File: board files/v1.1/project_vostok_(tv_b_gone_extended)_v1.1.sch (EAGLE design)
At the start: 25 parts, among them IC1 ATMEGA644PV-10PU, IC2 MCP1825S-3302E_DB, Q5 MPS2907A, T1 2N3904, T2 2N3904, T3 2N3904, T4 2N3904, U1 PEC11R-4015F-S0024

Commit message: modify port
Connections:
- removed net N$1: PORTC.10
- removed net N$2: PORTA.10
- new net N$4: R3.2, S1.2
- net GND: now also PORTA.2, PORTC.2
- net PA0: now also PORTA.10; no longer PORTA.1
- net PA1: now also PORTA.9; no longer PORTA.2
- net PA2: now also PORTA.8; no longer PORTA.3
- net PA3: now also PORTA.7; no longer PORTA.4
- net PA4: now also PORTA.6; no longer PORTA.5
- net PA5: now also PORTA.5; no longer PORTA.6
- net PA6: now also PORTA.4; no longer PORTA.7
- net PA7: now also PORTA.3; no longer PORTA.8
- net PC0: now also PORTC.10; no longer PORTC.1
- net PC1: now also PORTC.9; no longer PORTC.2
- net PC2: now also PORTC.8; no longer PORTC.3
- net PC3: now also PORTC.7; no longer PORTC.4
- net PC4: now also PORTC.6; no longer PORTC.5
- net PC5: now also PORTC.5; no longer PORTC.6
- net PC6: now also PORTC.4; no longer PORTC.7
- net PC7: now also PORTC.3; no longer PORTC.8
- net RESET: no longer R3.2, S1.2
- net VOUT_REG: now also PORTA.1, PORTC.1; no longer PORTA.9, PORTC.9

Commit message: add usb
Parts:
- added R5, R6: 68, rcl:R-EU_0204/7
- added R7: 1.5K, rcl:R-EU_0204/7
- added X1: MINI-USB_SHIELD5P2-32005-601, con-cypressindustries:MINI-USB_SHIELD5P2-32005-601
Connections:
- removed net N$11: IC1.PD0
- removed net N$12: IC1.PD1
- new net N$1: X1G41.1
- new net N$2: R5.1, X1G41.3
- new net N$5: X1G41.4
- new net N$6: R6.1, R7.1, X1G41.2
- new net PD0: IC1.PD0, R2.1
- new net PD1: IC1.PD1, R1.1, U1.1
- net GND: now also X1G41.5
- net PB2: now also R5.2; no longer R1.1, U1.1
- net PB3: now also R6.2; no longer R2.1
- net VIN_REG: now also R7.2
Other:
- note added: "D+"
- note added: "D-"
- note added: "GND"
- note added: "ID"
- note added: "USB"
- note added: "VCC"
- moved on the sheet: BAT_1, IC2

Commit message: add voltage pin to USB
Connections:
- removed net N$1: X1G41.1
- net VIN_REG: now also X1G41.1
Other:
- note added: "FLOATING"
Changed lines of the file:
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@@
 <?xml version="1.0" encoding="utf-8"?>
 <!DOCTYPE eagle SYSTEM "eagle.dtd">
-<eagle version="8.6.0">
+<eagle version="9.1.3">
 <drawing>
 <settings>
@@
 <text x="17.78" y="156.464" size="1.778" layer="95">D-</text>
 <text x="15.748" y="154.178" size="1.778" layer="95">VCC</text>
+<text x="38.1" y="162.56" size="1.778" layer="95">FLOATING</text>
 </plain>
 <instances>
@@
 <instance part="GND6" gate="1" x="200.66" y="304.8"/>
 <instance part="GND10" gate="1" x="200.66" y="281.94"/>
-<instance part="X1" gate="G41" x="27.94" y="160.02" rot="R180"/>
+<instance part="X1" gate="G41" x="27.94" y="160.02" smashed="yes" rot="R180">
+<attribute name="VALUE" x="17.78" y="167.64" size="1.778" layer="96" rot="R270"/>
+</instance>
 <instance part="R5" gate="G$1" x="53.34" y="149.86" smashed="yes" rot="R270">
 <attribute name="NAME" x="54.61" y="149.8346" size="1.778" layer="95"/>
@@
 <label x="76.2" y="157.48" size="1.778" layer="95"/>
 </segment>
+<segment>
+<pinref part="X1" gate="G41" pin="1"/>
+<wire x1="33.02" y1="154.94" x2="38.1" y2="154.94" width="0.1524" layer="91"/>
+<wire x1="38.1" y1="154.94" x2="38.1" y2="147.32" width="0.1524" layer="91"/>
+<label x="38.1" y="147.32" size="1.778" layer="95" rot="R180"/>
+</segment>
 </net>
 <net name="PB0" class="0">
@@
 </segment>
 </net>
-<net name="N$1" class="0">
-<segment>
-<pinref part="X1" gate="G41" pin="1"/>
-<wire x1="33.02" y1="154.94" x2="38.1" y2="154.94" width="0.1524" layer="91"/>
-<wire x1="38.1" y1="154.94" x2="38.1" y2="147.32" width="0.1524" layer="91"/>
-</segment>
-</net>

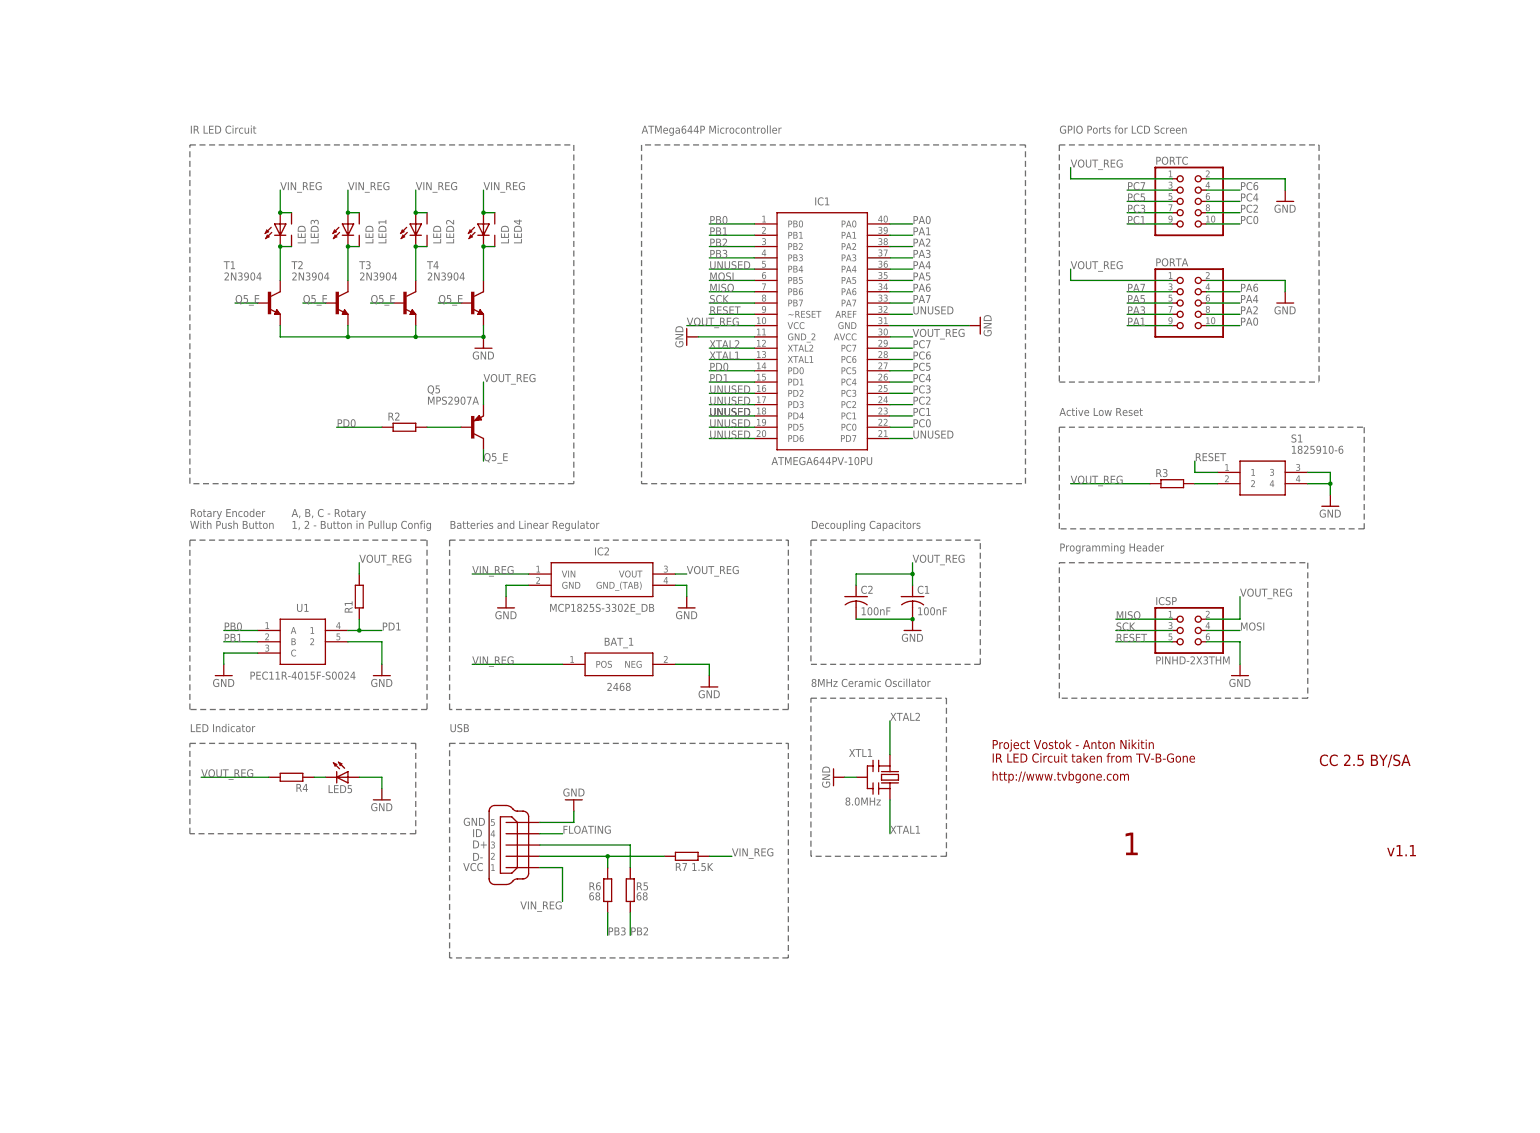
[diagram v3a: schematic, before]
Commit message: modify pin assignments for rotary encoder
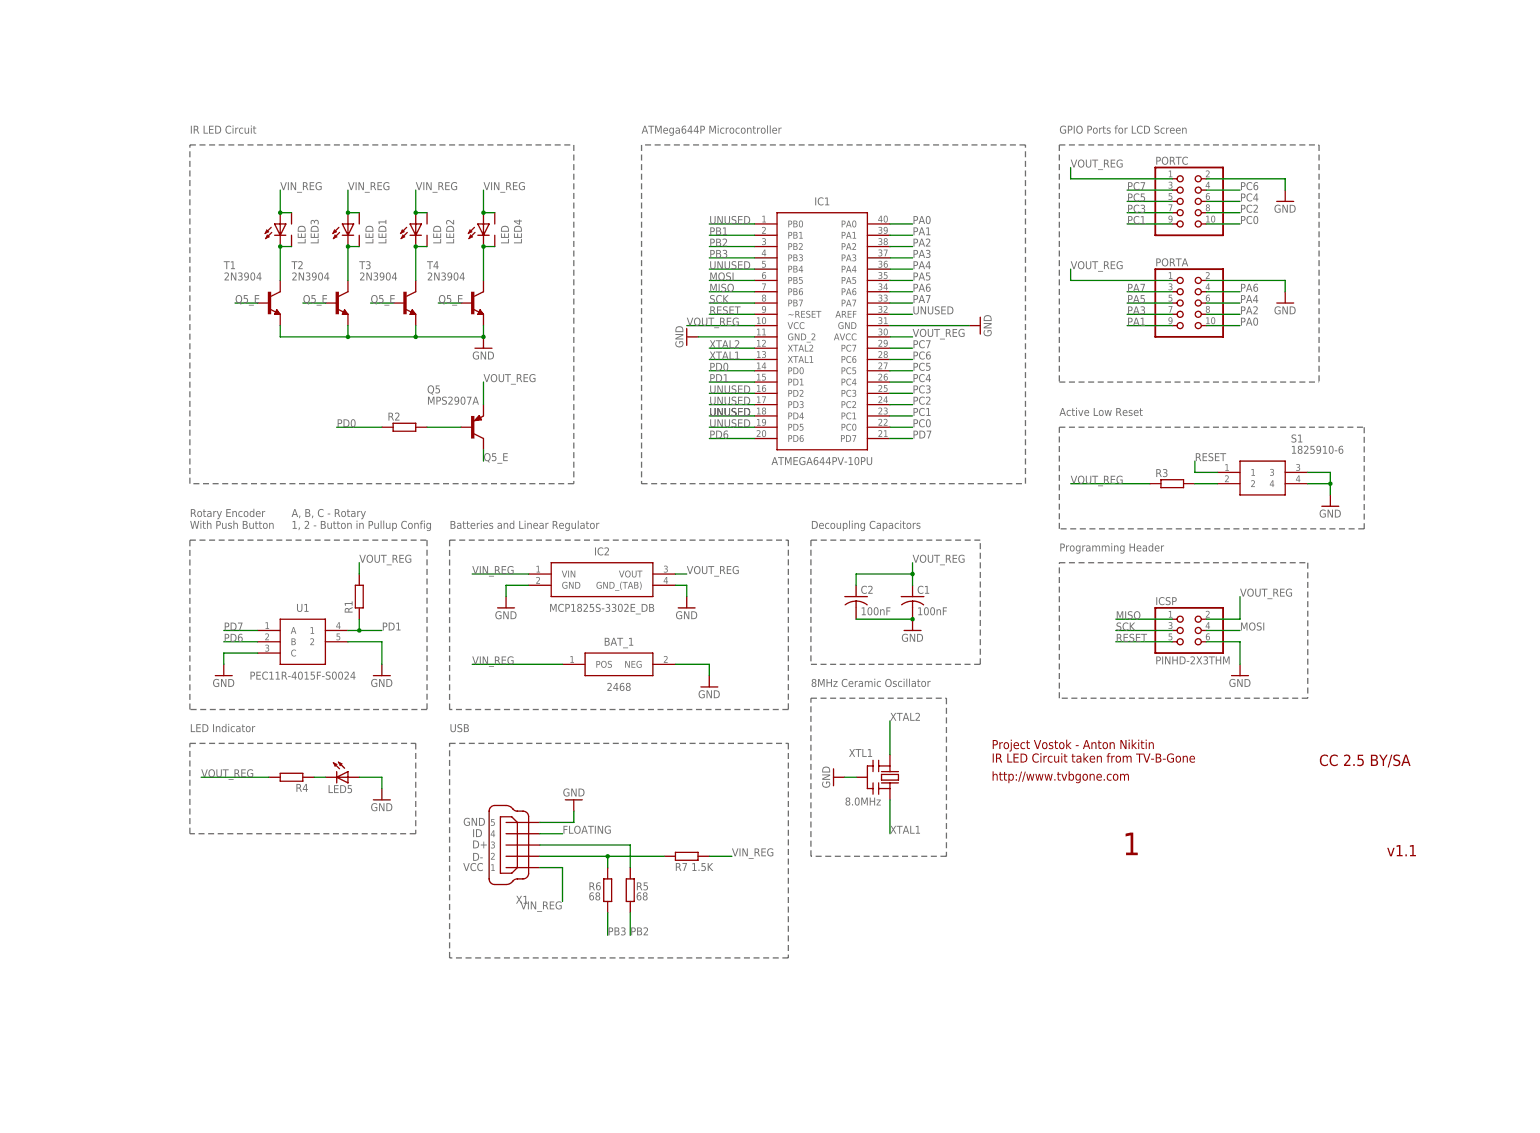
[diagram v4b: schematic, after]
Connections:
- removed net N$17: IC1.PD6
- removed net N$19: IC1.PD7
- removed net PB0: IC1.PB0, U1.A
- removed net PB1: IC1.PB1, U1.B
- new net N$1: IC1.PB0
- new net PD6: IC1.PD6, U1.B
- new net PD7: IC1.PD7, U1.A
- new net UNUSED: IC1.PB1
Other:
- note removed: "PB0"

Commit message: update schematic and update pdf
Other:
- note removed: "1"
- moved on the sheet: BAT_1, C1, C2, IC1, IC2, ICSP, LED1, LED2, LED3, LED4, LED5, PORTA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
